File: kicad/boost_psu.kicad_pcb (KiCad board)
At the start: 2 copper layers, 40 x 35 mm, 18 parts, among them J1 +12V, J2 HT, Q1 MPSA55, Q2 IRF740, U1 MC34063AP

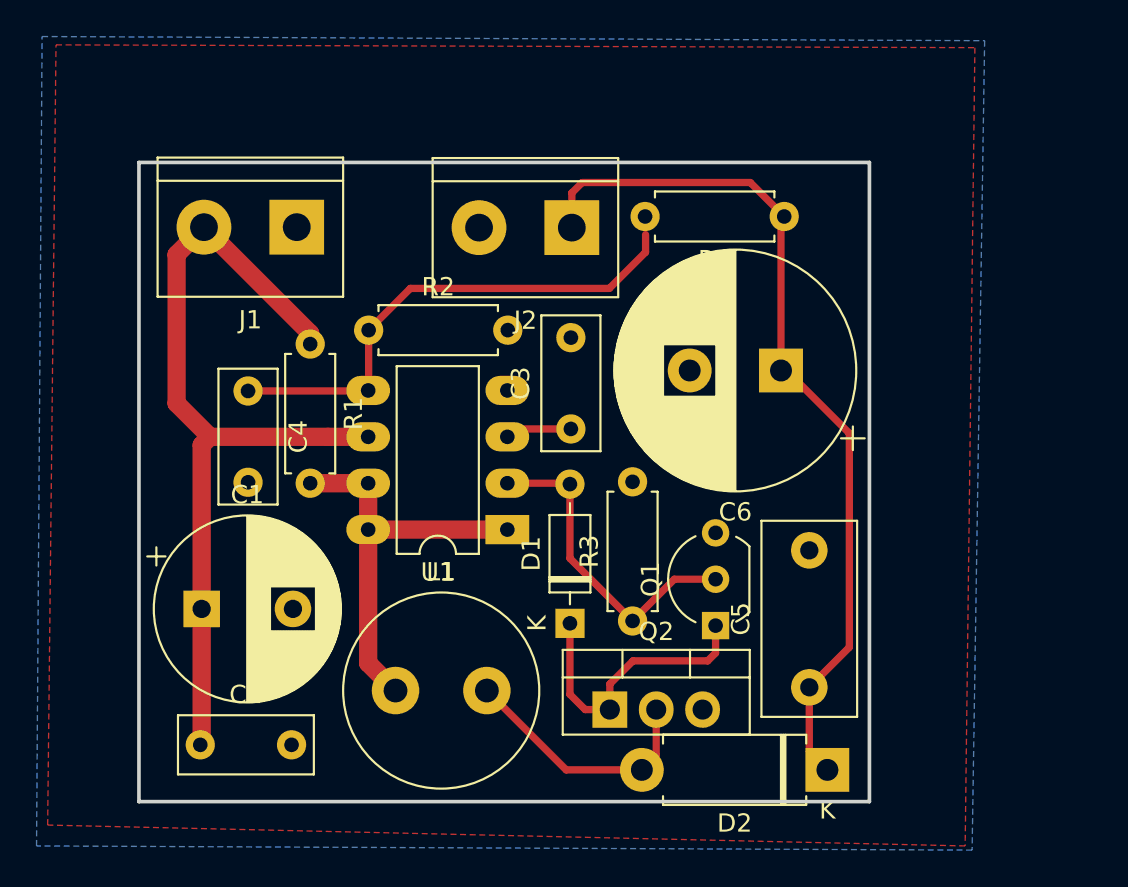
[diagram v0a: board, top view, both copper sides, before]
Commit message: Improve schematic & PCB routing
- put filtering capacitors on the switch collector rather than Vin
- add a 100n filtering capacitor on Vin
- switch to a 30x50mm board for a better layout
- add LEMON Amps as co-author

Signed-off-by: Arnaud Ferraris <arnaud.ferraris@gmail.com>
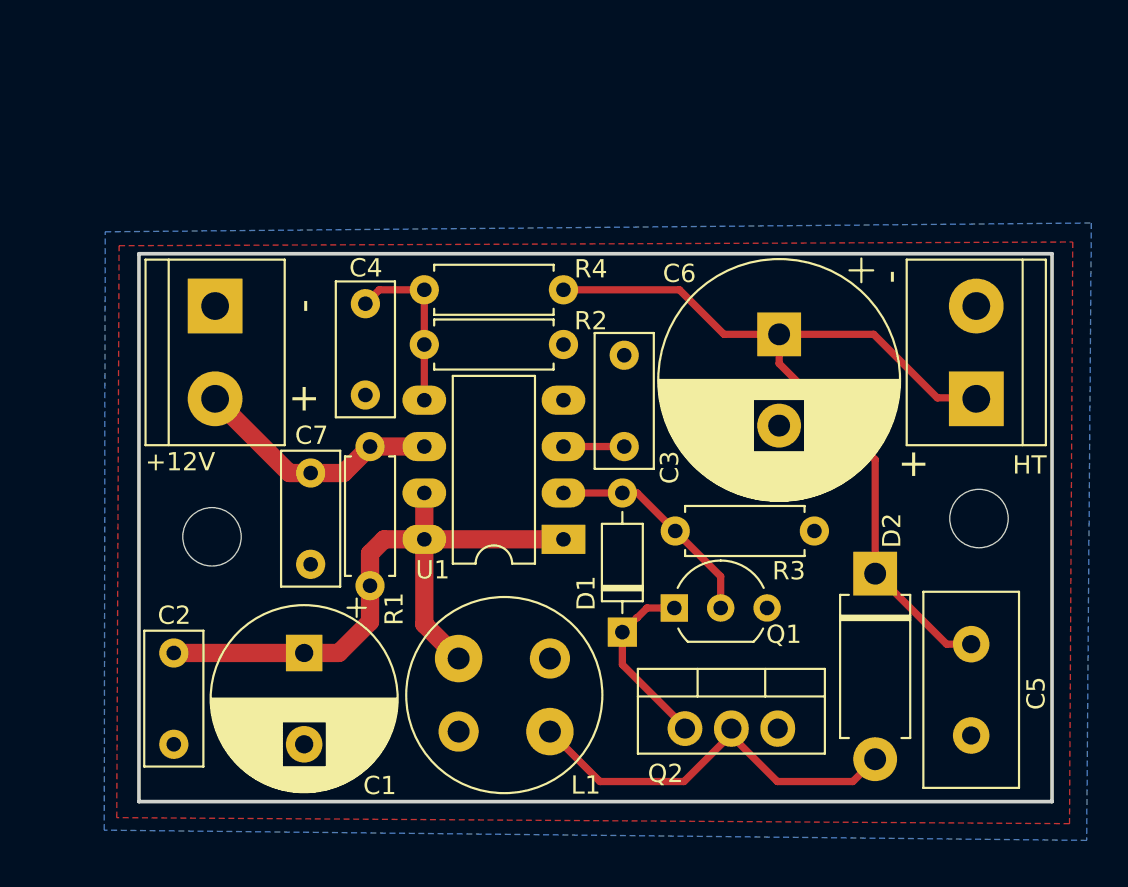
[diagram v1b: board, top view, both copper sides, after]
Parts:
- added C7: 100n, Capacitor_THT:C_Rect_L7.2mm_W3.0mm_P5.00mm_FKS2_FKP2_MKS2_MKP2, F.Cu at (149.4, 102.0)
- added REF**: MountingHole_3.2mm_M3, MountingHole:MountingHole_3.2mm_M3, F.Cu at (186.0, 104.5)
- added REF**: MountingHole_3.2mm_M3, MountingHole:MountingHole_3.2mm_M3, F.Cu at (144.0, 105.5)
- C5: footprint Capacitor_THT:C_Disc_D10.5mm_W5.0mm_P7.50mm -> Capacitor_THT:C_Disc_D10.5mm_W5.0mm_P5.00mm
- L1: footprint Inductor_THT:L_Radial_D10.5mm_P5.00mm_Abacron_AISR-01 -> ProjectLib:L_Radial_D10.5mm_P5.00mm_MuRATA_1200RS
- moved J2 24.1 mm to (185.9, 97.9), turned to 90 degrees
- moved R4 12.7 mm to (163.2, 92.0)
- moved D2 11.1 mm to (180.3, 107.5), turned to 270 degrees
- moved C5 9.17 mm to (185.6, 111.4), turned to 270 degrees
- moved C4 8.01 mm to (152.4, 92.7)
- moved R1 6.50 mm to (152.7, 100.6)
- moved J1 6.22 mm to (144.2, 92.9), turned to 270 degrees
- moved C1 6.11 mm to (149.0, 111.9), turned to 270 degrees
- moved R3 5.45 mm to (169.4, 105.2), turned to 0 degrees
- moved C2 5.23 mm to (141.9, 111.9), turned to 270 degrees
- moved Q2 4.24 mm to (169.9, 116.0)
- moved L1 3.87 mm to (157.5, 112.2), turned to 90 degrees
- moved R2 3.15 mm to (155.6, 95.0)
- moved U1 3.12 mm to (163.2, 105.6)
- moved C3 3.08 mm to (166.6, 100.6)
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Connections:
- C1 pad 1: /IN -> /PEAK
- C2 pad 1: /IN -> /PEAK
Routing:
- net /IN: track 47.4 -> 13.7 mm
- net Net-(C4-Pad1): track 27.8 -> 9.59 mm
- net /PEAK: track 22.8 -> 36.0 mm
- net /HT1: track 13.9 -> 22.3 mm
- net Net-(D1-Pad1): track 15.8 -> 10.1 mm
- net Net-(D1-Pad2): track 17.9 -> 12.2 mm
- net /HT2: track 48.0 -> 47.1 mm
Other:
- board size 40 x 35 mm -> 50 x 30 mm
- board text added: "+"
- board text added: "-"

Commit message: Change IRF740 orientation
As the MPSA55 is pretty close, it is better for the IRF740 tab to face
outwards, in order not to dissipate heat towards the transistor.

Signed-off-by: Arnaud Ferraris <arnaud.ferraris@gmail.com>
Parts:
- moved Q2 5.08 mm to (175.0, 116.0), turned to 180 degrees
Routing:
- net Net-(D1-Pad1): track 10.1 -> 13.6 mm
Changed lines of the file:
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@@
     (thickness 1.6)
     (drawings 8)
-    (tracks 53)
+    (tracks 55)
     (zones 0)
     (modules 21)
@@
   )
   (module Package_TO_SOT_THT:TO-220-3_Vertical (layer F.Cu)
-    (at 169.9006 116.0018)
+    (at 174.9806 116.0018 180)
     (descr "TO-220-3, Vertical, RM 2.54mm, see https://www.vishay.com/docs/66542/to-220-1.pdf")
     (tags "TO-220-3 Vertical RM 2.54mm")
-    (fp_text reference Q2 (at -1.0668 2.4638) (layer F.SilkS)
-      (effects (font (size 1 1) (thickness 0.15)))
-    )
-    (fp_text value IRF740 (at 2.54 2.5) (layer F.Fab)
+    (fp_text reference Q2 (at -1.0668 2.4638 180) (layer F.SilkS)
+      (effects (font (size 1 1) (thickness 0.15)))
+    )
+    (fp_text value IRF740 (at 2.54 2.5 180) (layer F.Fab)
       (effects (font (size 1 1) (thickness 0.15)))
     )
@@
     (fp_line (start 7.79 1.51) (end 7.79 -3.4) (layer F.CrtYd) (width 0.05))
     (fp_line (start 7.79 -3.4) (end -2.71 -3.4) (layer F.CrtYd) (width 0.05))
-    (fp_text user %R (at 2.54 -4.27) (layer F.Fab)
-      (effects (font (size 1 1) (thickness 0.15)))
-    )
-    (pad 1 thru_hole circle (at 0 0) (size 1.905 1.905) (drill 1.1) (layers *.Cu *.Mask)
+    (fp_text user %R (at 2.54 -4.27 180) (layer F.Fab)
+      (effects (font (size 1 1) (thickness 0.15)))
+    )
+    (pad 1 thru_hole circle (at 0 0 180) (size 1.905 1.905) (drill 1.1) (layers *.Cu *.Mask)
       (net 4 "Net-(D1-Pad1)"))
-    (pad 2 thru_hole oval (at 2.54 0) (size 1.905 2) (drill 1.1) (layers *.Cu *.Mask)
+    (pad 2 thru_hole oval (at 2.54 0 180) (size 1.905 2) (drill 1.1) (layers *.Cu *.Mask)
       (net 8 /HT1))
-    (pad 3 thru_hole oval (at 5.08 0) (size 1.905 2) (drill 1.1) (layers *.Cu *.Mask)
+    (pad 3 thru_hole oval (at 5.08 0 180) (size 1.905 2) (drill 1.1) (layers *.Cu *.Mask)
       (net 1 GND))
     (model ${KISYS3DMOD}/Package_TO_SOT_THT.3dshapes/TO-220-3_Vertical.wrl
@@
   (segment (start 169.3164 109.3978) (end 167.8178 109.3978) (width 0.4) (layer F.Cu) (net 4))
   (segment (start 167.8178 109.3978) (end 167.2844 109.9312) (width 0.4) (layer F.Cu) (net 4))
-  (segment (start 169.9006 115.9256) (end 169.9006 116.0018) (width 0.4) (layer F.Cu) (net 4))
-  (segment (start 166.4716 110.7186) (end 166.4716 112.4966) (width 0.4) (layer F.Cu) (net 4))
-  (segment (start 166.4716 112.4966) (end 169.9006 115.9256) (width 0.4) (layer F.Cu) (net 4))
+  (segment (start 169.3164 110.5478) (end 171.189 112.4204) (width 0.4) (layer F.Cu) (net 4))
+  (segment (start 169.3164 109.3978) (end 169.3164 110.5478) (width 0.4) (layer F.Cu) (net 4))
+  (segment (start 171.189 112.4204) (end 173.355 112.4204) (width 0.4) (layer F.Cu) (net 4))
+  (segment (start 174.9806 114.046) (end 174.9806 116.0018) (width 0.4) (layer F.Cu) (net 4))
+  (segment (start 173.355 112.4204) (end 174.9806 114.046) (width 0.4) (layer F.Cu) (net 4))
   (segment (start 163.2458 103.0986) (end 166.4716 103.0986) (width 0.4) (layer F.Cu) (net 5))
   (segment (start 167.2844 103.0986) (end 169.3672 105.1814) (width 0.4) (layer F.Cu) (net 5))

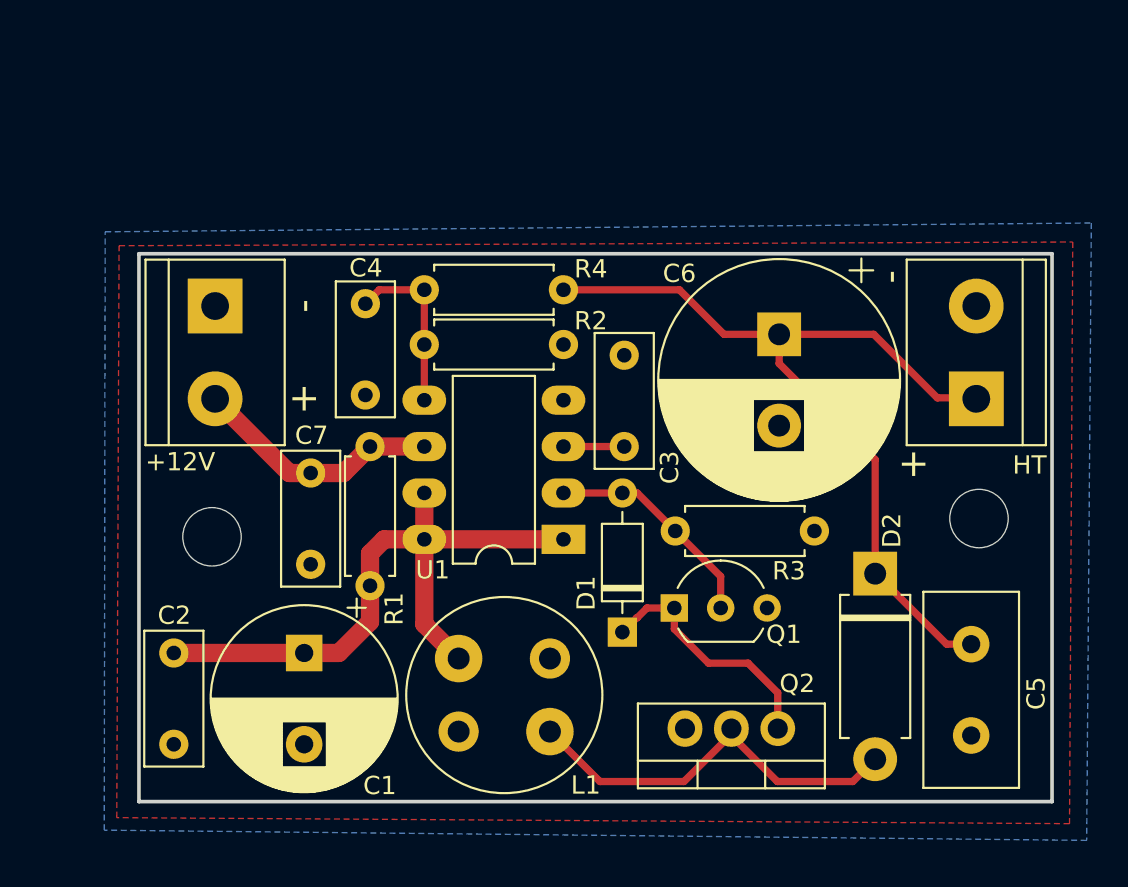
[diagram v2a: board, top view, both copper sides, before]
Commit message: Change a few footprints and rework schematics
Signed-off-by: Arnaud Ferraris <arnaud.ferraris@gmail.com>
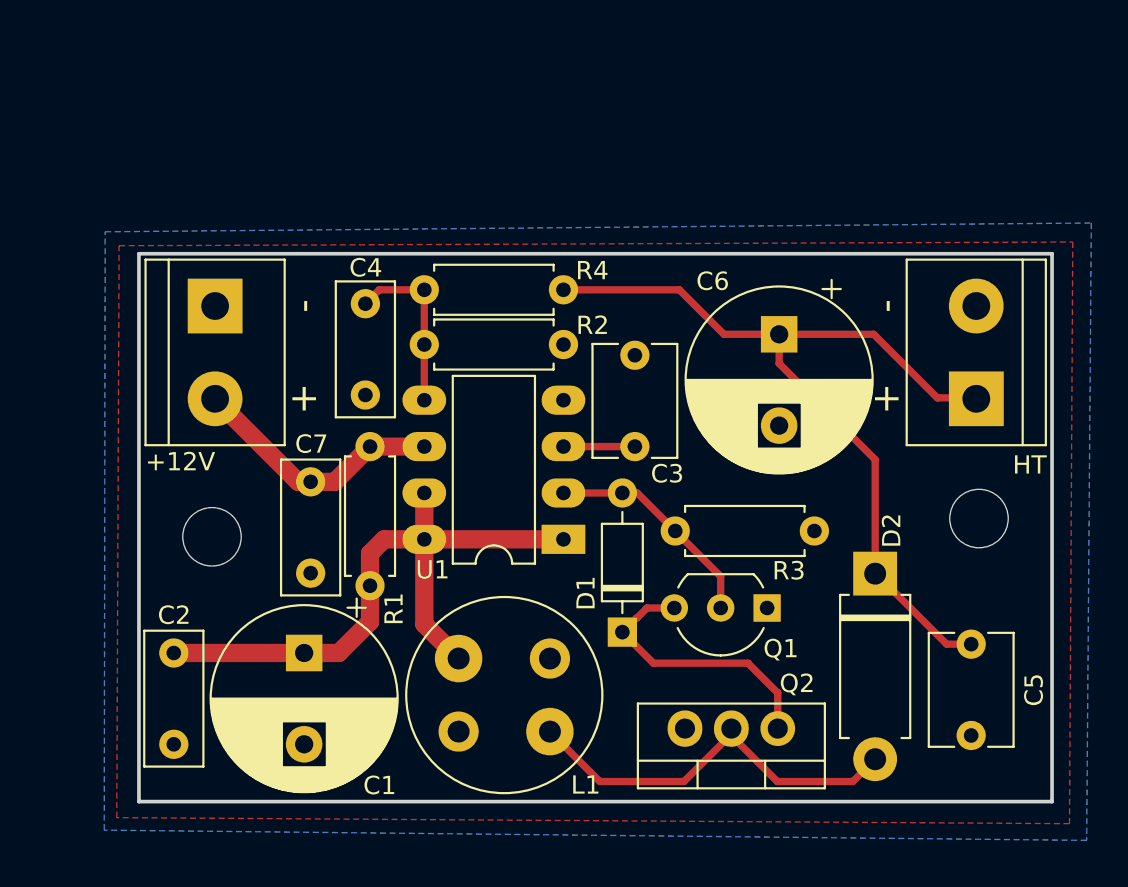
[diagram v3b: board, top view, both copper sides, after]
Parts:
- C3: footprint Capacitor_THT:C_Rect_L7.2mm_W3.0mm_P5.00mm_FKS2_FKP2_MKS2_MKP2 -> Capacitor_THT:C_Disc_D6.0mm_W4.4mm_P5.00mm
- C4: value 10n -> 100n
- C5: value 100n -> 10n/400V; footprint Capacitor_THT:C_Disc_D10.5mm_W5.0mm_P5.00mm -> Capacitor_THT:C_Disc_D6.0mm_W4.4mm_P5.00mm
- C6: footprint Capacitor_THT:CP_Radial_D13.0mm_P5.00mm -> Capacitor_THT:CP_Radial_D10.0mm_P5.00mm
- D1: value 1N914 -> 1N4148
- Q1: value MPSA55 -> MPS751
- moved Q1 5.08 mm to (174.4, 109.4), turned to 180 degrees
- moved C3 0.58 mm to (167.2, 100.6)
- moved C7 0.48 mm to (149.4, 102.5)
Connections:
- Q1 pad 1: Net-(D1-Pad1) -> GND
- Q1 pad 3: GND -> Net-(D1-Pad1)
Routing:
- net Net-(D1-Pad1): track 13.6 -> 15.2 mm

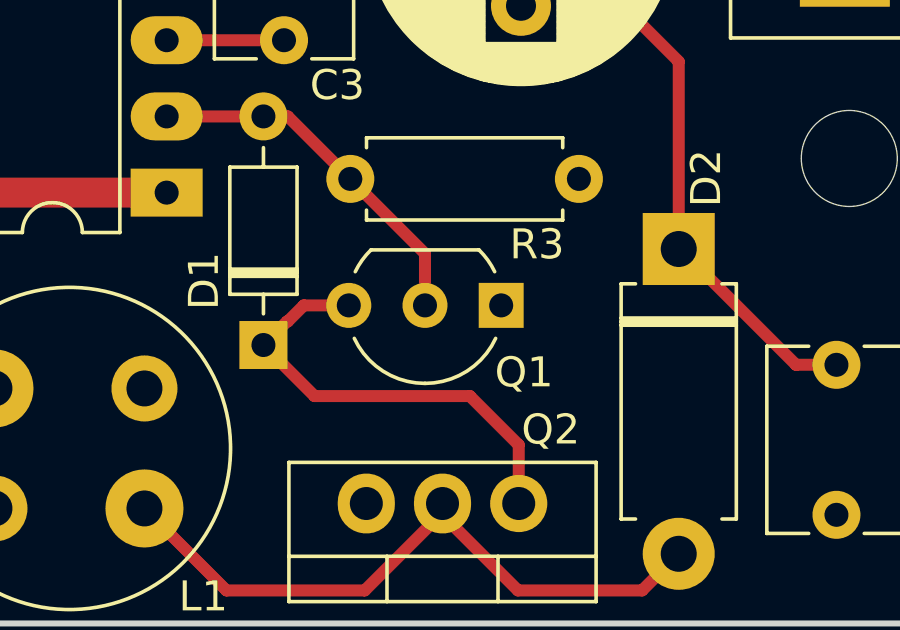
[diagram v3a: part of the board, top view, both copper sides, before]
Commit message: Fix transistor polarity
Signed-off-by: Arnaud Ferraris <arnaud.ferraris@gmail.com>
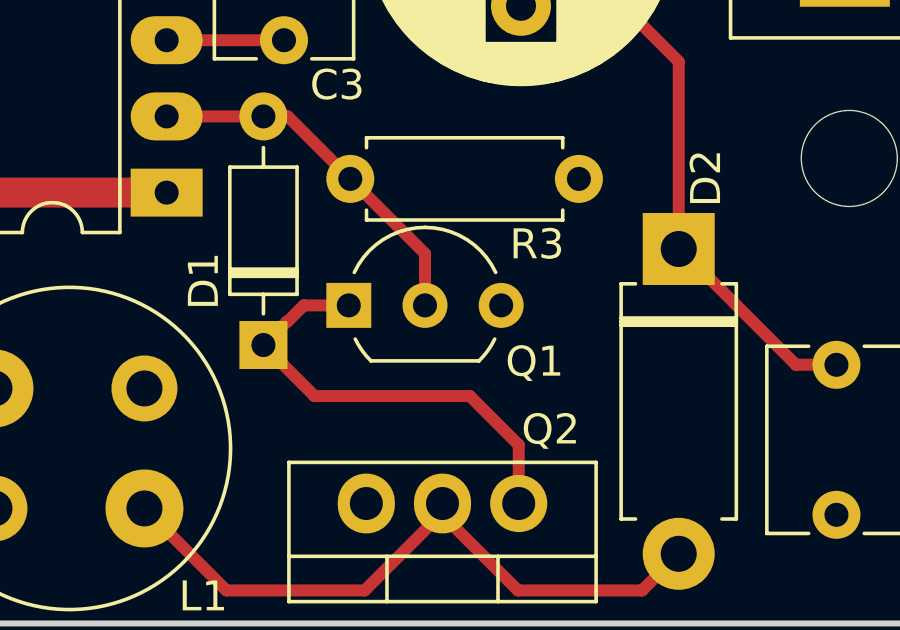
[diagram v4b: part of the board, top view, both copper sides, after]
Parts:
- moved Q1 5.08 mm to (169.3, 109.4), turned to 0 degrees
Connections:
- Q1 pad 1: GND -> Net-(D1-Pad1)
- Q1 pad 3: Net-(D1-Pad1) -> GND
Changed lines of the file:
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@@
   )
   (module Package_TO_SOT_THT:TO-92_Inline_Wide (layer F.Cu)
-    (at 174.3964 109.3978 180)
+    (at 169.3164 109.3978)
     (descr "TO-92 leads in-line, wide, drill 0.75mm (see NXP sot054_po.pdf)")
     (tags "to-92 sc-43 sc-43a sot54 PA33 transistor")
-    (fp_text reference Q1 (at -0.762 -2.2352 180) (layer F.SilkS)
+    (fp_text reference Q1 (at 6.1976 1.8796) (layer F.SilkS)
       (effects (font (size 1 1) (thickness 0.15)))
     )
-    (fp_text value MPS751 (at 2.54 2.79 180) (layer F.Fab)
+    (fp_text value MPS751 (at 2.54 2.79) (layer F.Fab)
       (effects (font (size 1 1) (thickness 0.15)))
     )
-    (fp_text user %R (at 2.54 -3.56 180) (layer F.Fab)
+    (fp_text user %R (at 2.54 -3.56) (layer F.Fab)
       (effects (font (size 1 1) (thickness 0.15)))
     )
@@
     (fp_arc (start 2.54 0) (end 2.54 -2.48) (angle -135) (layer F.Fab) (width 0.1))
     (fp_arc (start 2.54 0) (end 4.34 1.85) (angle -20) (layer F.SilkS) (width 0.12))
-    (pad 2 thru_hole circle (at 2.54 0 270) (size 1.5 1.5) (drill 0.8) (layers *.Cu *.Mask)
+    (pad 2 thru_hole circle (at 2.54 0 90) (size 1.5 1.5) (drill 0.8) (layers *.Cu *.Mask)
       (net 5 "Net-(D1-Pad2)"))
-    (pad 3 thru_hole circle (at 5.08 0 270) (size 1.5 1.5) (drill 0.8) (layers *.Cu *.Mask)
+    (pad 3 thru_hole circle (at 5.08 0 90) (size 1.5 1.5) (drill 0.8) (layers *.Cu *.Mask)
+      (net 1 GND))
+    (pad 1 thru_hole rect (at 0 0 90) (size 1.5 1.5) (drill 0.8) (layers *.Cu *.Mask)
       (net 4 "Net-(D1-Pad1)"))
-    (pad 1 thru_hole rect (at 0 0 270) (size 1.5 1.5) (drill 0.8) (layers *.Cu *.Mask)
-      (net 1 GND))
     (model ${KISYS3DMOD}/Package_TO_SOT_THT.3dshapes/TO-92_Inline_Wide.wrl
       (at (xyz 0 0 0))
